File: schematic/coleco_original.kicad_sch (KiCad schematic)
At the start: 0 parts

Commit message: completed sound block, finished cart io port, and finished decoder.
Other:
- sheet clock_reset ports: added SND_CLK, VDP_CLK, ~{U18_G2}; removed none
- sheet controller ports: added ~{U18_G2}, ~{U19_G2}; removed none
- sheet io_ports ports: added SND_OUT, ~{VDP_RESET}; removed none
- sheet rf_mod ports: added SND_CLK, SND_OUT; removed none
- sheet sound ports: added SND_CLK, SND_OUT; removed none
- sheet video ports: added B-Y, R-Y, VDP_CLK, Y, ~{VDP_RESET}; removed none

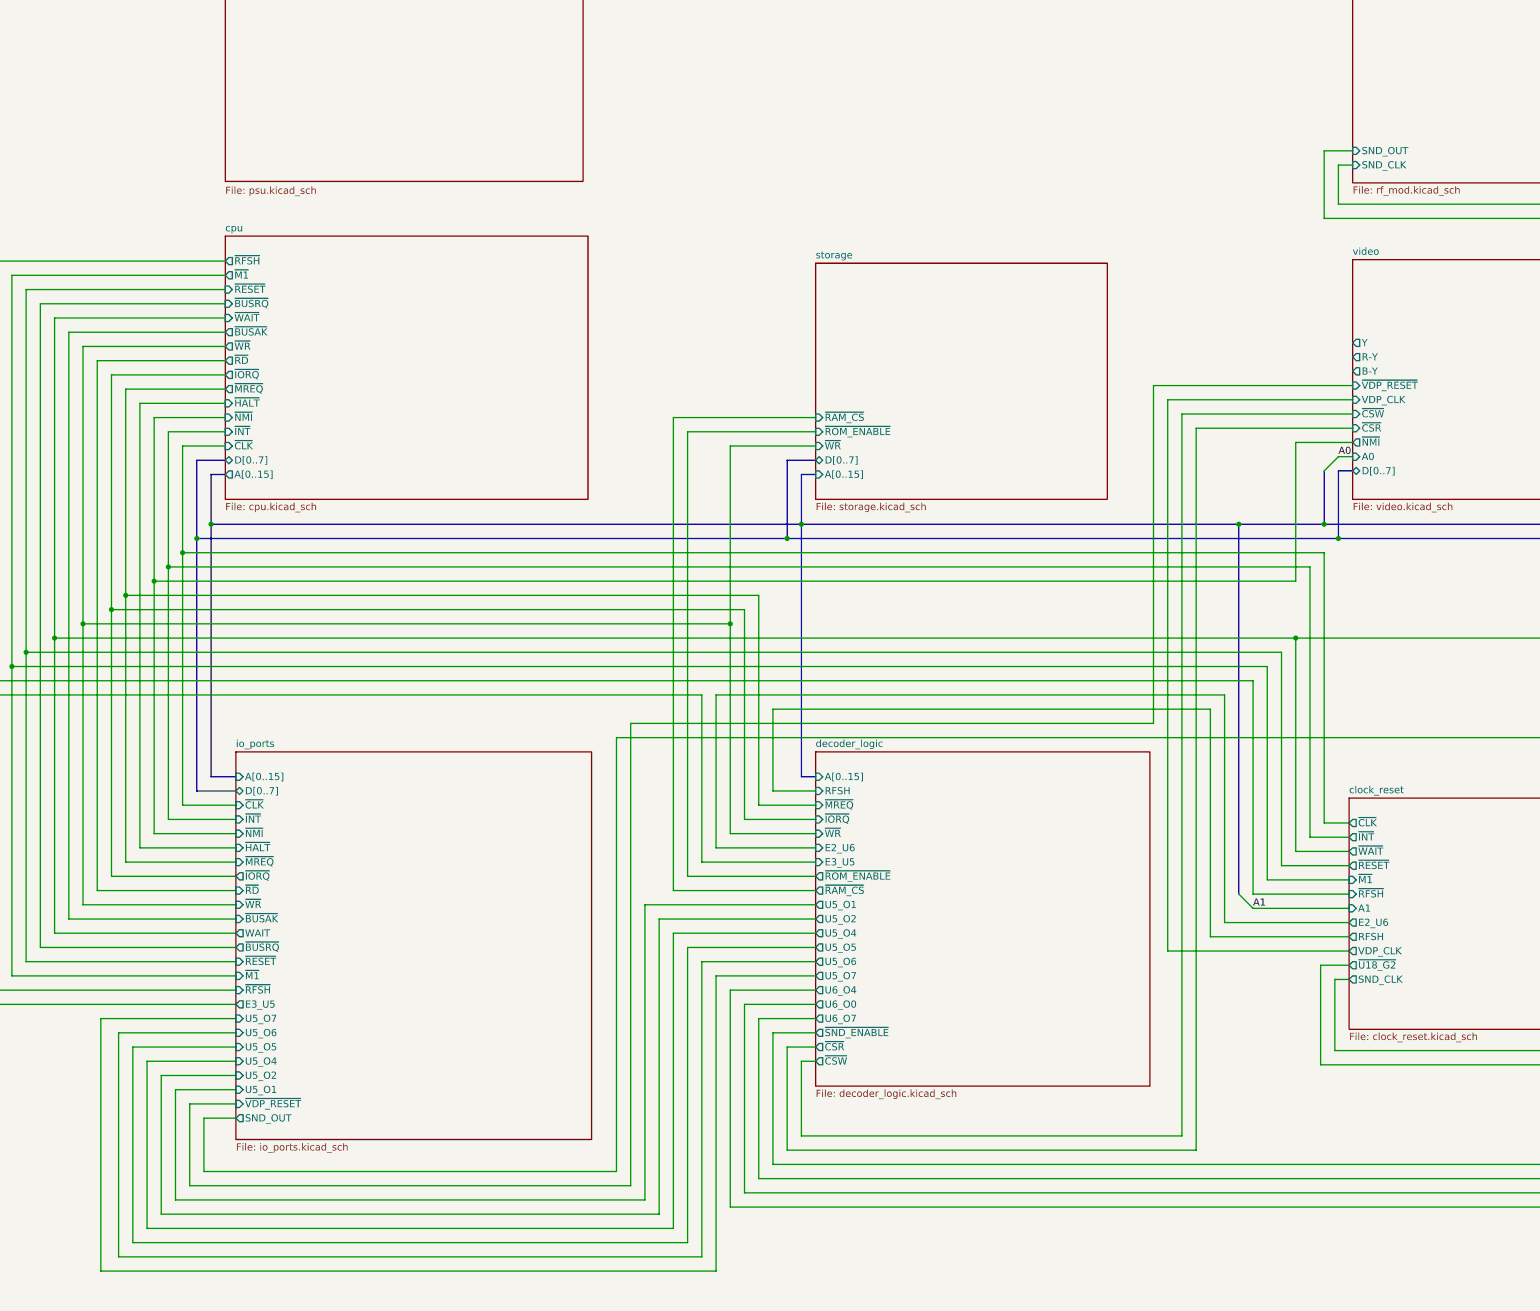
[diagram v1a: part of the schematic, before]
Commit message: fixed some more line names, added a expansion port io pin.
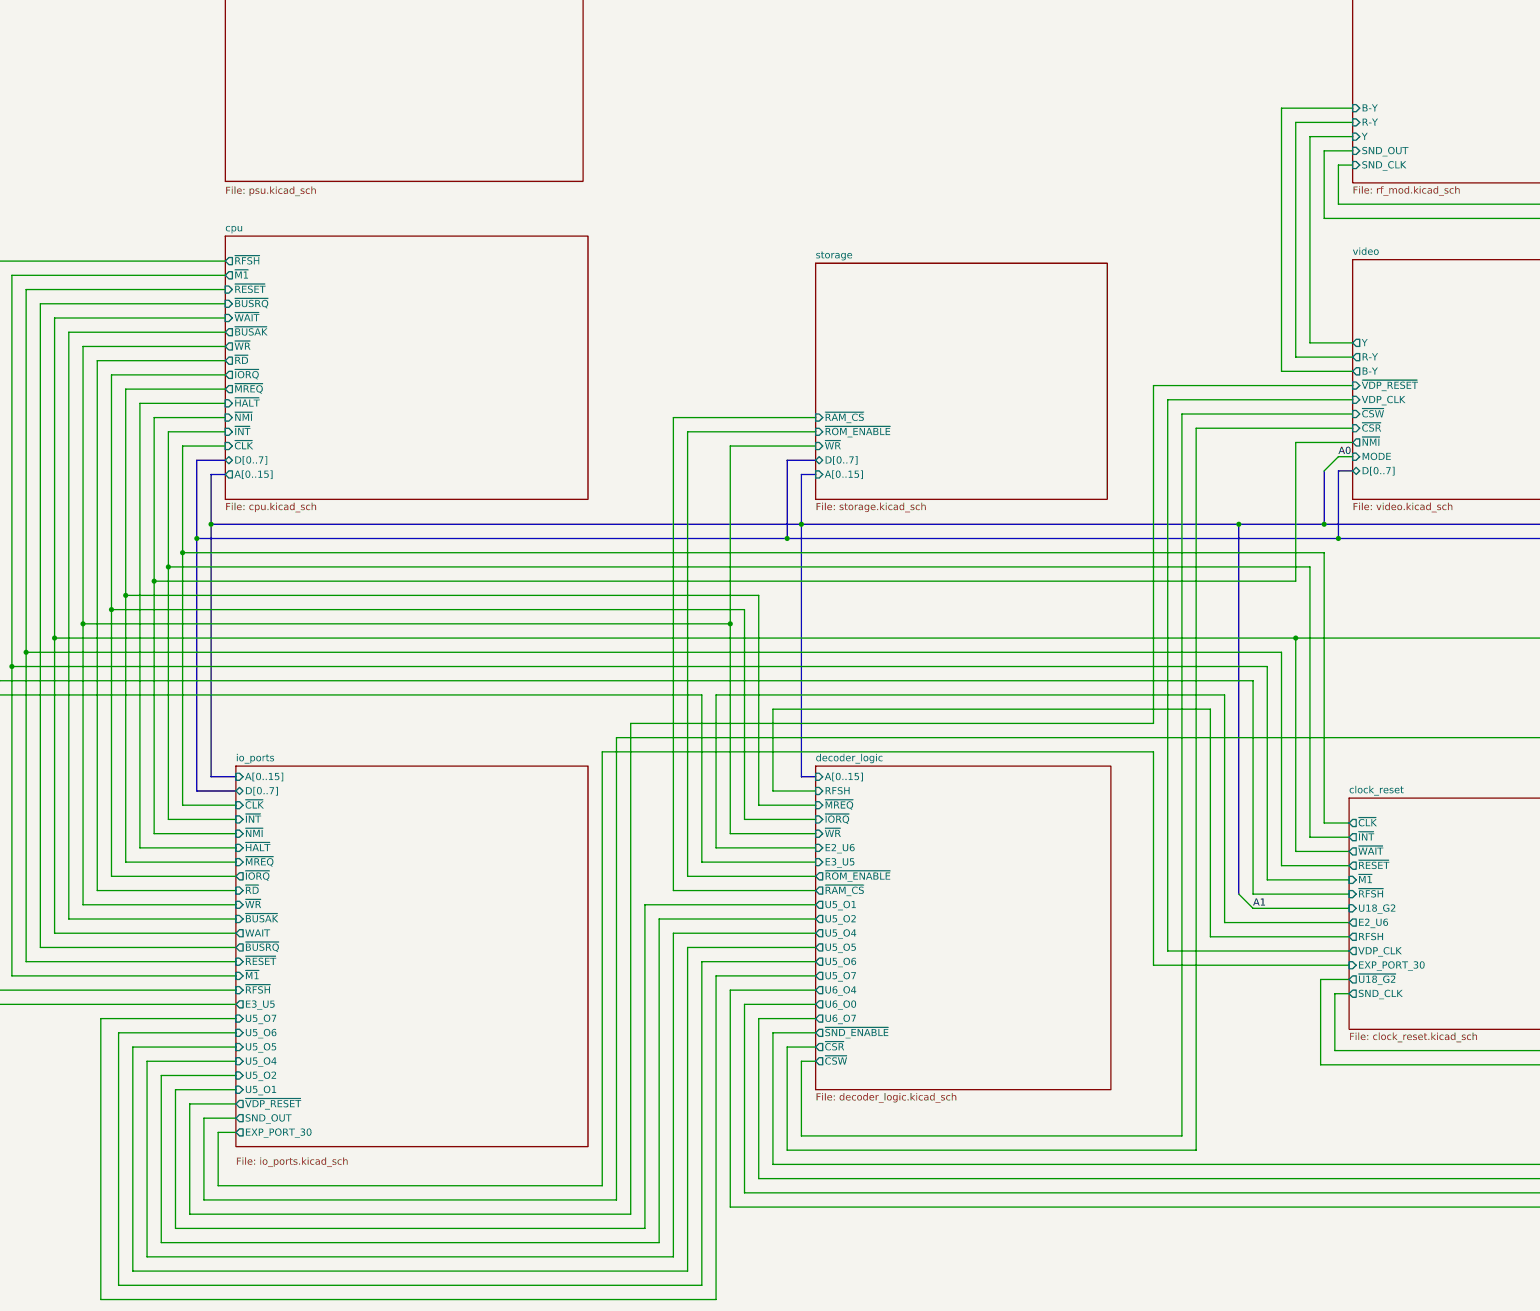
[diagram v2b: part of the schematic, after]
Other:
- sheet clock_reset ports: added EXP_PORT_30, U18_G2; removed A1
- sheet io_ports ports: added EXP_PORT_30; removed none
- sheet rf_mod ports: added B-Y, R-Y, Y; removed none
- sheet video ports: added MODE; removed A0

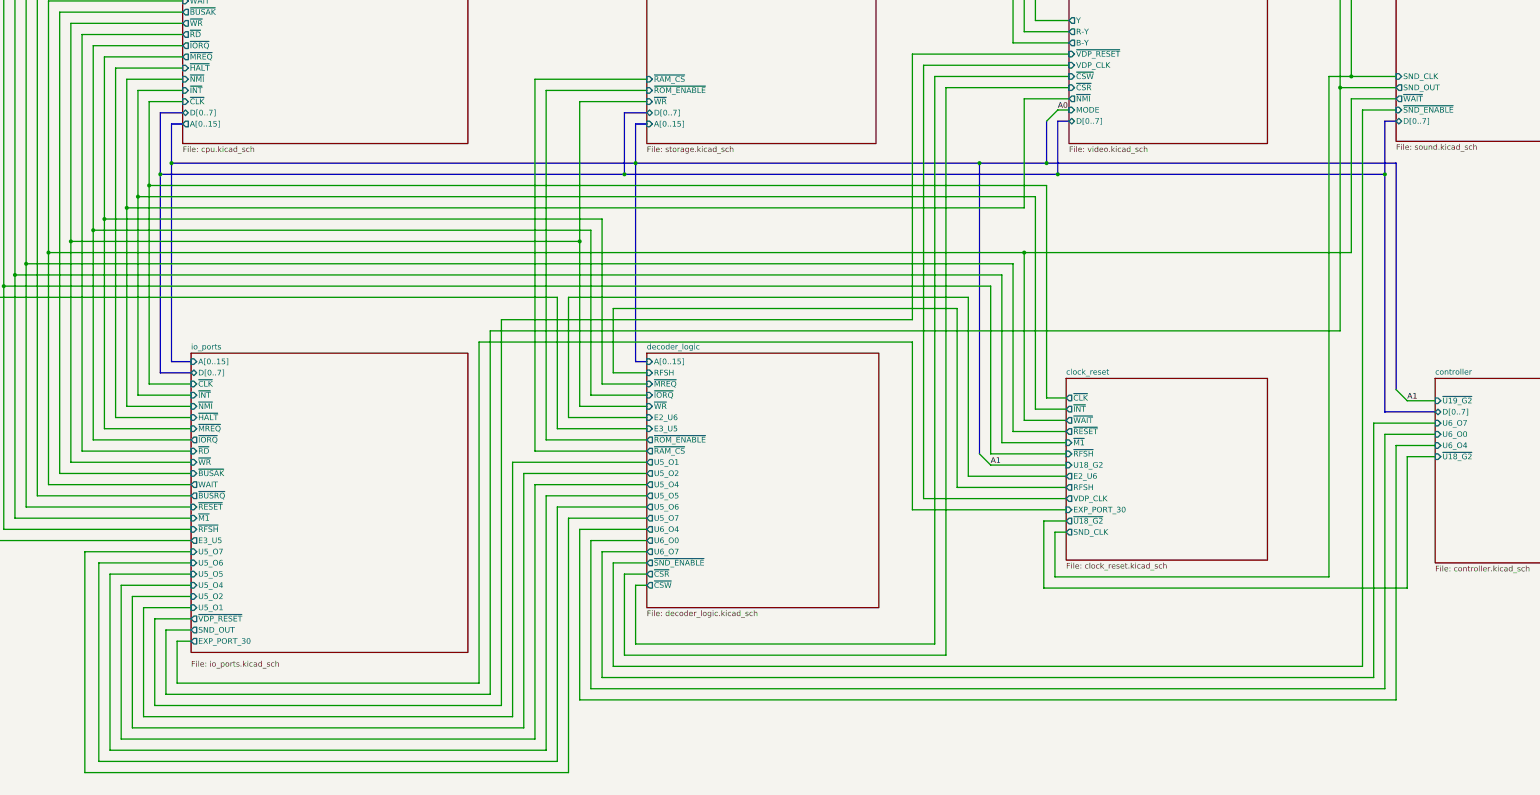
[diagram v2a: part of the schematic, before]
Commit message: power supply added, controller circuit added. Controller is a very odd duck to say the least. Seems they wanted to have plenty of current, maybe due to the steering wheel attachement?
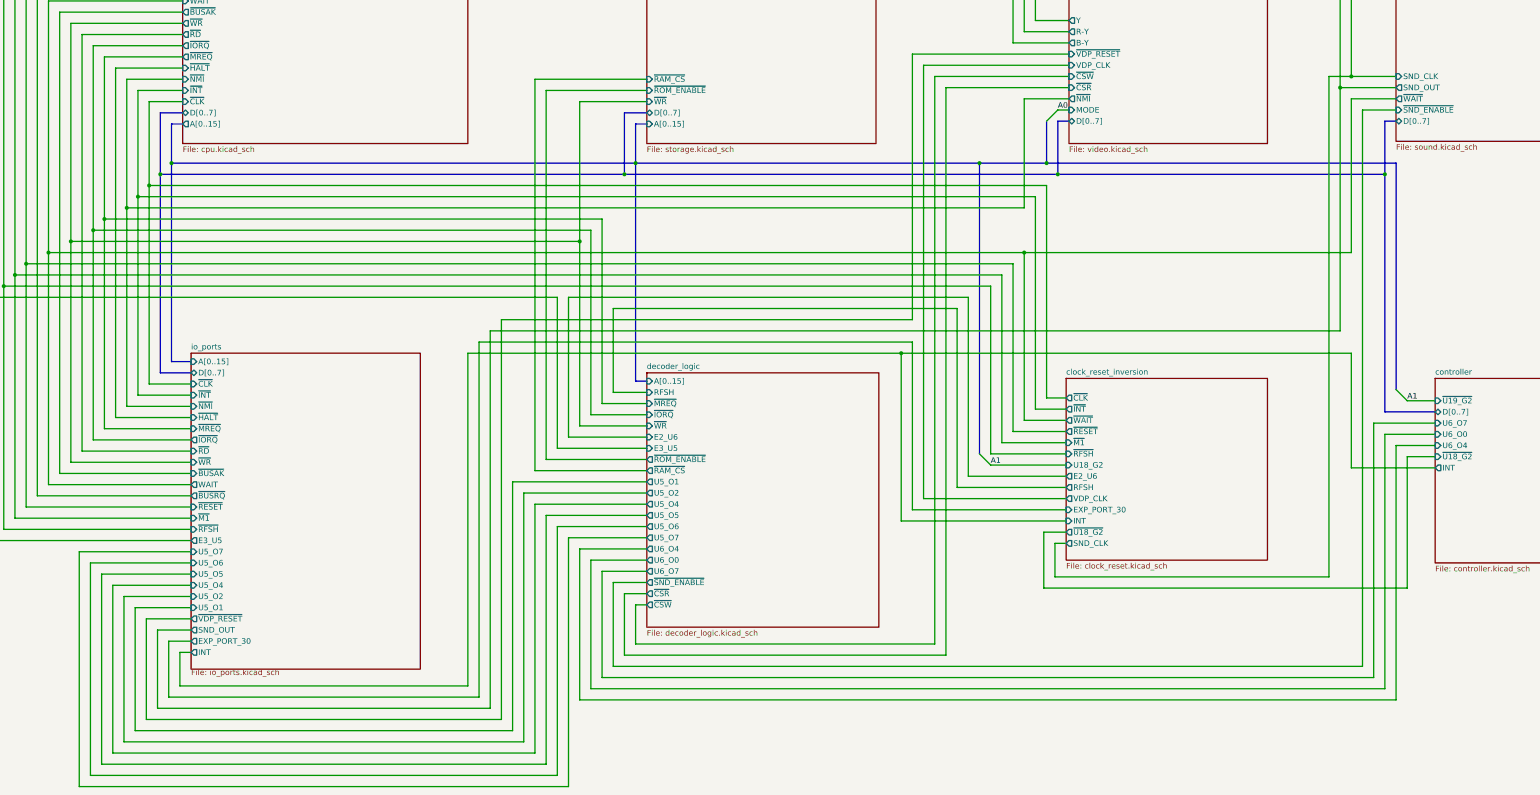
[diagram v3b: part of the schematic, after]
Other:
- sheet clock_reset renamed clock_reset_inversion
- sheet clock_reset_inversion ports: added INT; removed none
- sheet controller ports: added INT; removed none
- sheet io_ports ports: added INT; removed none

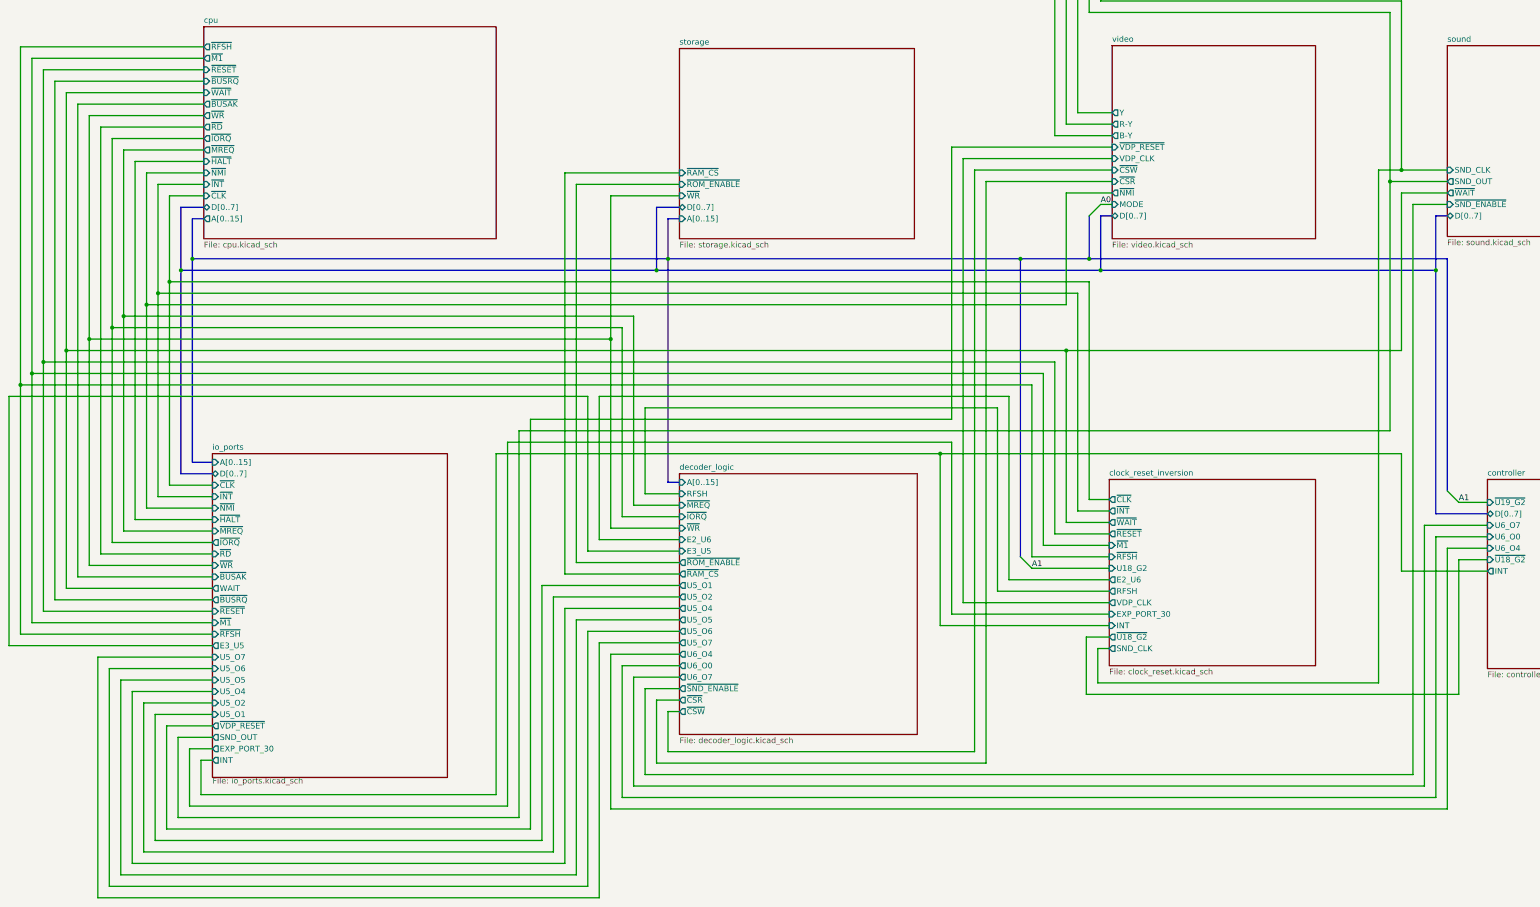
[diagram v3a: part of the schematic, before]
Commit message: started work on clock_reset_misc circuits. inverter u7 done, u8 added and starting work around U22.
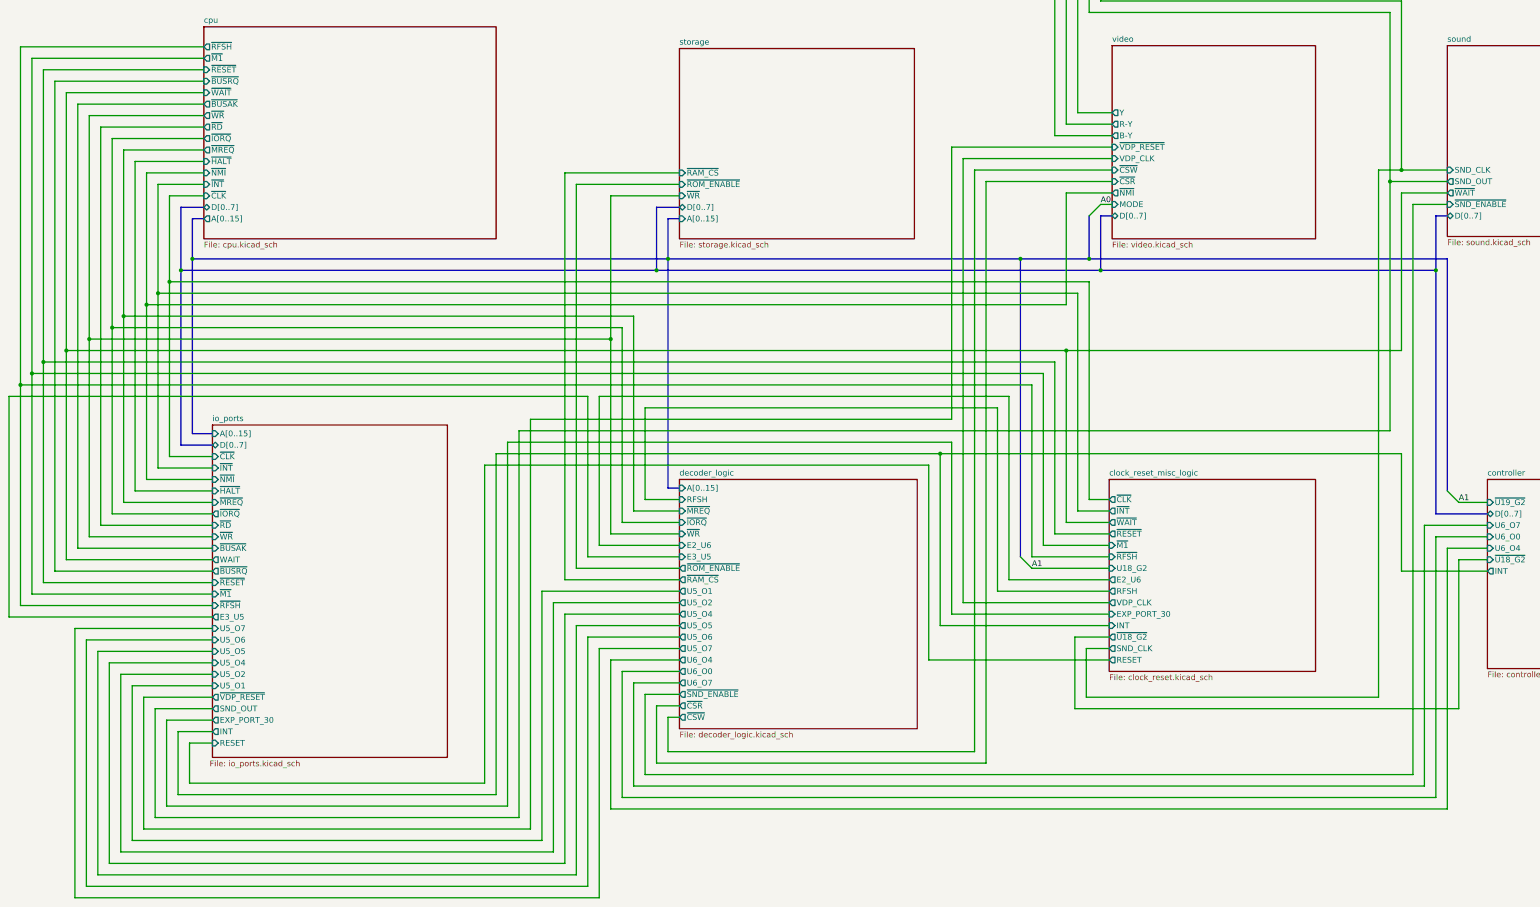
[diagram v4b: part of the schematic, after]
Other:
- sheet clock_reset_inversion renamed clock_reset_misc_logic
- sheet clock_reset_misc_logic ports: added RESET; removed none
- sheet io_ports ports: added RESET; removed none

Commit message: altered and did some cleanup of the way the wires were run. Finished expansion port routes to rf modulator. Added ext_psu for future external power supply design (will be an off the shelf psu block).
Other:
- sheet clock_reset_misc_logic ports: added EXP_RESET; removed none
- sheet io_ports ports: added EXP_PORT_31, EXP_PORT_32, EXP_PORT_33, EXP_RESET, SND_CLK; removed none
- sheet rf_mod ports: added EXP_PORT_31, EXP_PORT_32, EXP_PORT_33; removed none
